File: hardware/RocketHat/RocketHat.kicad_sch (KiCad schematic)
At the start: 29 parts, among them J1 Conn_02x16_Top_Bottom, J2 Conn_02x16_Top_Bottom, Q2 MMBT2222A, U1 BMP390, U2 BMI088, U3 ADXL375BCCZ, U5 74HC688, U6 74HC245, U7 74HC245, U8 MAX-M10S

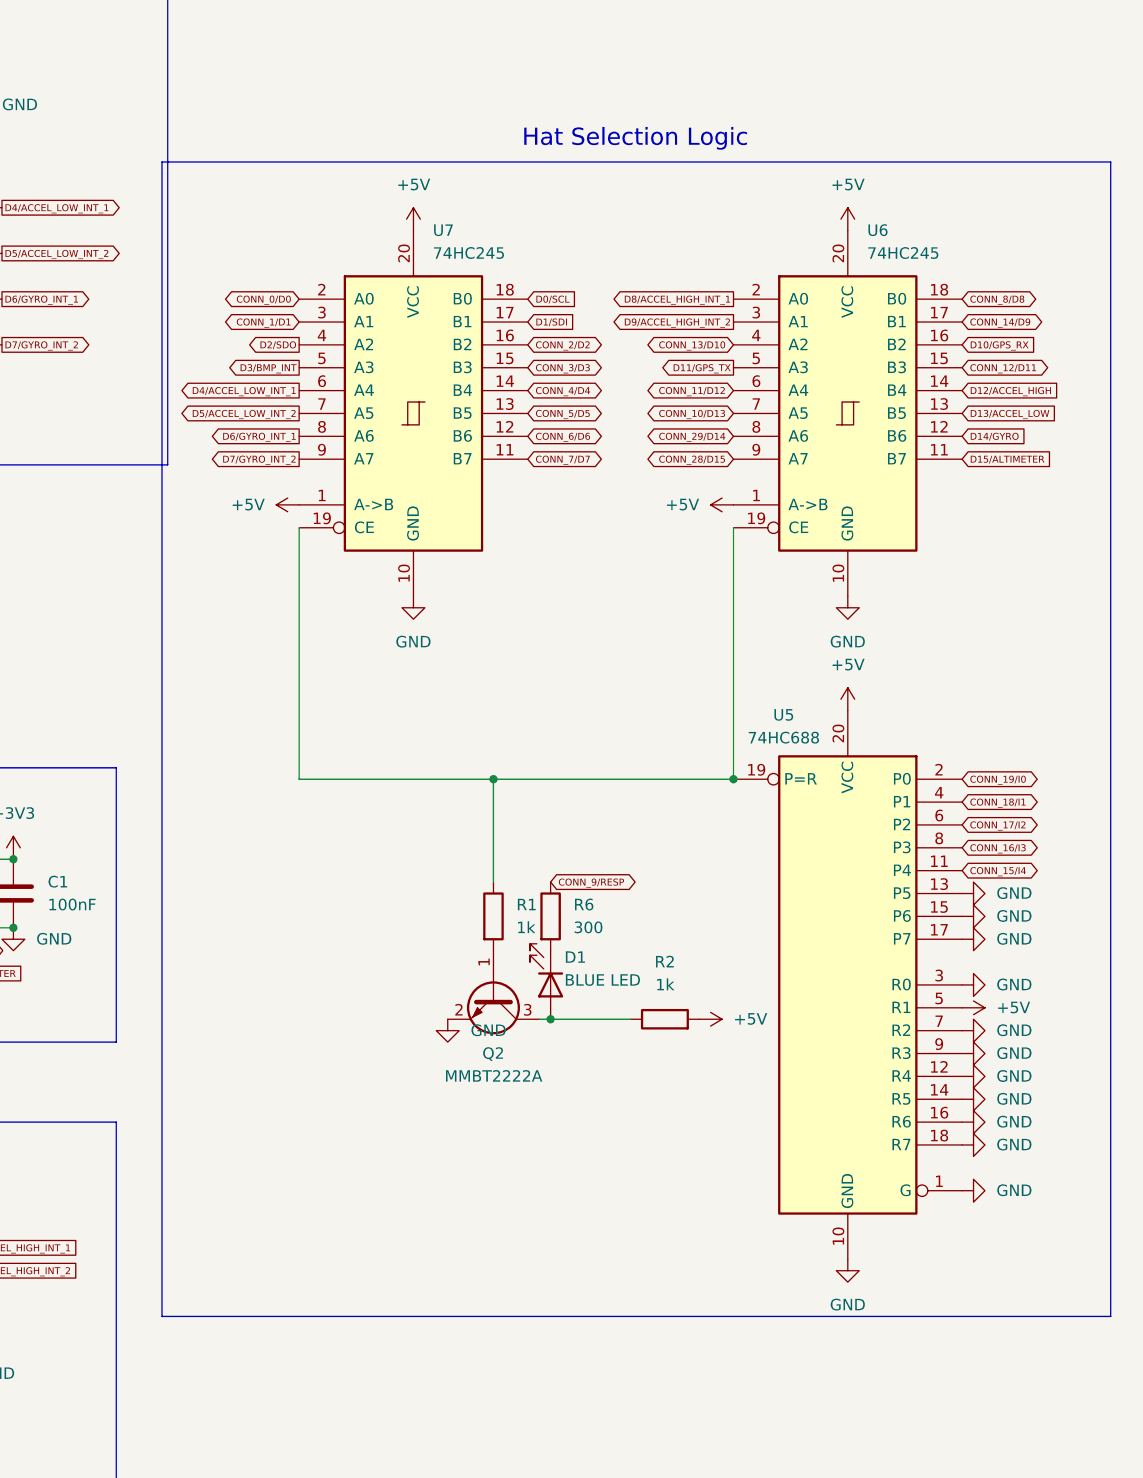
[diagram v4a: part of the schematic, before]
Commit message: Work more on traces for rocket hat and add dipswitch
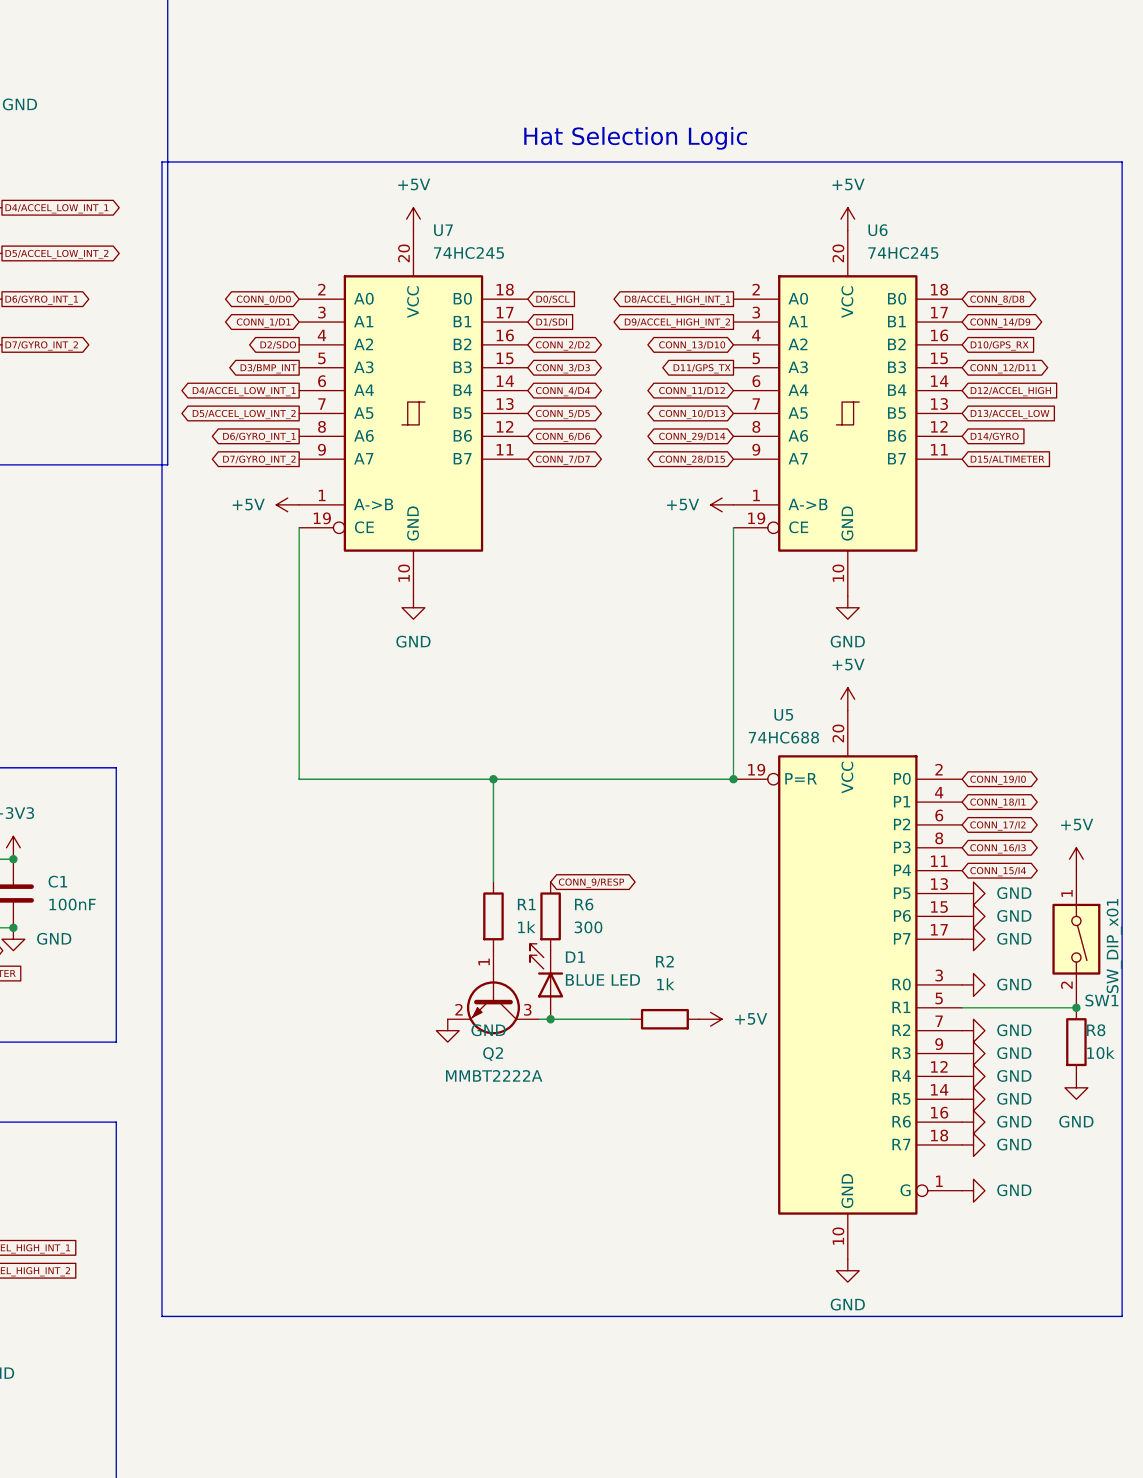
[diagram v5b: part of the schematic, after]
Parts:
- added R8: 10k, Resistor_SMD:R_0201_0603Metric, symbol Device:R
- added SW1: SW_DIP_x01, Button_Switch_SMD:SW_DIP_SPSTx01_Slide_Copal_CHS-01A_W5.08mm_P1.27mm_JPin, symbol Switch:SW_DIP_x01
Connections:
- net +5V: now also SW1.1; no longer U5.5 (R1)
- net GND: now also R8.2
- new net: R8.1, SW1.2, U5.5 (R1)
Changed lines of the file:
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@@
 	(rectangle
 		(start 176.53 38.1)
-		(end 281.94 166.37)
+		(end 283.21 166.37)
 		(stroke
 			(width 0)
@@
 	)
 	(junction
+		(at 278.13 132.08)
+		(diameter 0)
+		(color 0 0 0 0)
+	)
+	(junction
 		(at 76.2 46.99)
 		(diameter 0)
@@
 	(wire
 		(pts
+			(xy 265.43 132.08) (xy 278.13 132.08)
+		)
+		(stroke
+			(width 0)
+			(type default)
+		)
+	)
+	(wire
+		(pts
 			(xy 218.44 133.35) (xy 219.71 133.35)
 		)
@@
 	)
 	(symbol
-		(lib_id "power:+5V")
-		(at 265.43 132.08 270)
-		(unit 1)
-		(exclude_from_sim no)
-		(in_bom yes)
-		(on_board yes)
-		(dnp no)
-		(fields_autoplaced yes)
-		(property "Reference" "#PWR012"
-			(at 261.62 132.08 0)
-			(effects
-				(font
-					(size 1.27 1.27)
-				)
-				(hide yes)
-			)
-		)
-		(property "Value" "+5V"
-			(at 269.24 132.0799 90)
-			(effects
-				(font
-					(size 1.27 1.27)
-				)
-				(justify left)
-			)
-		)
-		(property "Footprint" ""
-			(at 265.43 132.08 0)
-			(effects
-				(font
-					(size 1.27 1.27)
-				)
-				(hide yes)
-			)
-		)
-		(property "Datasheet" ""
-			(at 265.43 132.08 0)
-			(effects
-				(font
-					(size 1.27 1.27)
-				)
-				(hide yes)
-			)
-		)
-		(property "Description" "Power symbol creates a global label with name \"+5V\""
-			(at 265.43 132.08 0)
-			(effects
-				(font
-					(size 1.27 1.27)
-				)
-				(hide yes)
-			)
-		)
-		(pin "1"
-		)
-		(instances
-			(project ""
-				(path "/988df97c-fca1-40e2-af98-331e3f3f354f"
-					(reference "#PWR012")
-					(unit 1)
-				)
-			)
-		)
-	)
-	(symbol
 		(lib_id "Device:R")
 		(at 76.2 43.18 0)
@@
 	)
 	(symbol
+		(lib_id "Device:R")
+		(at 278.13 135.89 0)
+		(unit 1)
+		(exclude_from_sim no)
+		(in_bom yes)
+		(on_board yes)
+		(dnp no)
+		(property "Reference" "R8"
+			(at 279.146 134.62 0)
+			(effects
+				(font
+					(size 1.27 1.27)
+				)
+				(justify left)
+			)
+		)
+		(property "Value" "10k"
+			(at 279.146 137.16 0)
+			(effects
+				(font
+					(size 1.27 1.27)
+				)
+				(justify left)
+			)
+		)
+		(property "Footprint" "Resistor_SMD:R_0201_0603Metric"
+			(at 276.352 135.89 90)
+			(effects
+				(font
+					(size 1.27 1.27)
+				)
+				(hide yes)
+			)
+		)
+		(property "Datasheet" "~"
+			(at 278.13 135.89 0)
+			(effects
+				(font
+					(size 1.27 1.27)
+				)
+				(hide yes)
+			)
+		)
+		(property "Description" "Resistor"
+			(at 278.13 135.89 0)
+			(effects
+				(font
+					(size 1.27 1.27)
+				)
+				(hide yes)
+			)
+		)
+		(pin "2"
+		)
+		(pin "1"
+		)
+		(instances
+			(project ""
+				(path "/988df97c-fca1-40e2-af98-331e3f3f354f"
+					(reference "R8")
+					(unit 1)
+				)
+			)
+		)
+	)
+	(symbol
 		(lib_id "Device:C")
 		(at 49.53 29.21 0)
@@
 	)
 	(symbol
+		(lib_id "power:+5V")
+		(at 278.13 116.84 0)
+		(unit 1)
+		(exclude_from_sim no)
+		(in_bom yes)
+		(on_board yes)
+		(dnp no)
+		(fields_autoplaced yes)
+		(property "Reference" "#PWR051"
+			(at 278.13 120.65 0)
+			(effects
+				(font
+					(size 1.27 1.27)
+				)
+				(hide yes)
+			)
+		)
+		(property "Value" "+5V"
+			(at 278.13 111.76 0)
+			(effects
+				(font
+					(size 1.27 1.27)
+				)
+			)
+		)
+		(property "Footprint" ""
+			(at 278.13 116.84 0)
+			(effects
+				(font
+					(size 1.27 1.27)
+				)
+				(hide yes)
+			)
+		)
+		(property "Datasheet" ""
+			(at 278.13 116.84 0)
+			(effects
+				(font
+					(size 1.27 1.27)
+				)
+				(hide yes)
+			)
+		)
+		(property "Description" "Power symbol creates a global label with name \"+5V\""
+			(at 278.13 116.84 0)
+			(effects
+				(font
+					(size 1.27 1.27)
+				)
+				(hide yes)
+			)
+		)
+		(pin "1"
+		)
+		(instances
+			(project "RocketHat"
+				(path "/988df97c-fca1-40e2-af98-331e3f3f354f"
+					(reference "#PWR051")
+					(unit 1)
+				)
+			)
+		)
+	)
+	(symbol
 		(lib_id "Device:C")
 		(at 76.2 50.8 0)
@@
 	)
 	(symbol
+		(lib_id "power:GND")
+		(at 278.13 139.7 0)
+		(unit 1)
+		(exclude_from_sim no)
+		(in_bom yes)
+		(on_board yes)
+		(dnp no)
+		(fields_autoplaced yes)
+		(property "Reference" "#PWR012"
+			(at 278.13 146.05 0)
+			(effects
+				(font
+					(size 1.27 1.27)
+				)
+				(hide yes)
+			)
+		)
+		(property "Value" "GND"
+			(at 278.13 144.78 0)
+			(effects
+				(font
+					(size 1.27 1.27)
+				)
+			)
+		)
+		(property "Footprint" ""
+			(at 278.13 139.7 0)
+			(effects
+				(font
+					(size 1.27 1.27)
+				)
+				(hide yes)
+			)
+		)
+		(property "Datasheet" ""
+			(at 278.13 139.7 0)
+			(effects
+				(font
+					(size 1.27 1.27)
+				)
+				(hide yes)
+			)
+		)
+		(property "Description" "Power symbol creates a global label with name \"GND\" , ground"
+			(at 278.13 139.7 0)
+			(effects
+				(font
+					(size 1.27 1.27)
+				)
+				(hide yes)
+			)
+		)
+		(pin "1"
+		)
+		(instances
+			(project "RocketHat"
+				(path "/988df97c-fca1-40e2-af98-331e3f3f354f"
+					(reference "#PWR012")
+					(unit 1)
+				)
+			)
+		)
+	)
+	(symbol
 		(lib_id "Device:R")
 		(at 219.71 121.92 0)
@@
 					(unit 1)
 				)
+			)
+		)
+	)
+	(symbol
+		(lib_id "Switch:SW_DIP_x01")
+		(at 278.13 124.46 270)
+		(unit 1)
+		(exclude_from_sim no)
+		(in_bom yes)
+		(on_board yes)
+		(dnp no)
+		(property "Reference" "SW1"
+			(at 282.956 131.318 90)
+			(effects
+				(font
+					(size 1.27 1.27)
+				)
+				(justify right)
+			)
+		)
+		(property "Value" "SW_DIP_x01"
+			(at 282.194 130.556 0)
+			(effects
+				(font
+					(size 1.27 1.27)
+				)
+				(justify right)
+			)
+		)
+		(property "Footprint" "Button_Switch_SMD:SW_DIP_SPSTx01_Slide_Copal_CHS-01A_W5.08mm_P1.27mm_JPin"
+			(at 278.13 124.46 0)
+			(effects
+				(font
+					(size 1.27 1.27)
+				)
+				(hide yes)
+			)
+		)
+		(property "Datasheet" "~"
+			(at 278.13 124.46 0)
+			(effects
+				(font
+					(size 1.27 1.27)
+				)
+				(hide yes)
+			)
+		)
+		(property "Description" "1x DIP Switch, Single Pole Single Throw (SPST) switch, small symbol"
+			(at 278.13 124.46 0)
+			(effects
+				(font
+					(size 1.27 1.27)
+				)
+				(hide yes)
+			)
+		)
+		(pin "2"
+		)
+		(pin "1"
+		)
+		(instances
+			(project ""
+				(path "/988df97c-fca1-40e2-af98-331e3f3f354f"
+					(reference "SW1")
+					(unit 1)
+				)

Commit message: rocket hat done
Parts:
- removed SW1: SW_DIP_x01, Button_Switch_SMD:SW_DIP_SPSTx01_Slide_Copal_CHS-01A_W5.08mm_P1.27mm_JPin, symbol Switch:SW_DIP_x01
- added TP1, TP2: TestPoint, TestPoint:TestPoint_Pad_1.5x1.5mm, symbol Connector:TestPoint
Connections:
- net +5V: now also TP2.1
- net at R8.1, U5.5 (R1): now also TP1.1
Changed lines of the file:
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@@
 	)
 	(junction
+		(at 278.13 132.08)
+		(diameter 0)
+		(color 0 0 0 0)
+	)
+	(junction
 		(at 82.55 163.83)
 		(diameter 0)
@@
 	)
 	(junction
-		(at 278.13 132.08)
-		(diameter 0)
-		(color 0 0 0 0)
-	)
-	(junction
 		(at 76.2 46.99)
 		(diameter 0)
@@
 	)
 	(symbol
+		(lib_id "Connector:TestPoint")
+		(at 278.13 132.08 0)
+		(unit 1)
+		(exclude_from_sim no)
+		(in_bom yes)
+		(on_board yes)
+		(dnp no)
+		(fields_autoplaced yes)
+		(property "Reference" "TP1"
+			(at 280.67 127.5079 0)
+			(effects
+				(font
+					(size 1.27 1.27)
+				)
+				(justify left)
+			)
+		)
+		(property "Value" "TestPoint"
+			(at 280.67 130.0479 0)
+			(effects
+				(font
+					(size 1.27 1.27)
+				)
+				(justify left)
+			)
+		)
+		(property "Footprint" "TestPoint:TestPoint_Pad_1.5x1.5mm"
+			(at 283.21 132.08 0)
+			(effects
+				(font
+					(size 1.27 1.27)
+				)
+				(hide yes)
+			)
+		)
+		(property "Datasheet" "~"
+			(at 283.21 132.08 0)
+			(effects
+				(font
+					(size 1.27 1.27)
+				)
+				(hide yes)
+			)
+		)
+		(property "Description" "test point"
+			(at 278.13 132.08 0)
+			(effects
+				(font
+					(size 1.27 1.27)
+				)
+				(hide yes)
+			)
+		)
+		(pin "1"
+		)
+		(instances
+			(project ""
+				(path "/988df97c-fca1-40e2-af98-331e3f3f354f"
+					(reference "TP1")
+					(unit 1)
+				)
+			)
+		)
+	)
+	(symbol
 		(lib_id "power:GND")
 		(at 153.67 171.45 0)
@@
 		(on_board yes)
 		(dnp no)
-		(fields_autoplaced yes)
 		(property "Reference" "#PWR037"
 			(at 133.35 67.31 0)
@@
 		)
 		(property "Value" "GND"
-			(at 135.89 62.2299 0)
+			(at 131.826 64.77 0)
 			(effects
 				(font
@@
 	)
 	(symbol
-		(lib_id "power:GND")
-		(at 265.43 121.92 90)
+		(lib_id "Connector:TestPoint")
+		(at 278.13 116.84 180)
 		(unit 1)
 		(exclude_from_sim no)
@@
 		(dnp no)
 		(fields_autoplaced yes)
-		(property "Reference" "#PWR02"
-			(at 271.78 121.92 0)
+		(property "Reference" "TP2"
+			(at 280.67 118.8719 0)
 			(effects
 				(font
 					(size 1.27 1.27)
 				)
-				(hide yes)
+				(justify right)
 			)
 		)
-		(property "Value" "GND"
-			(at 269.24 121.9199 90)
+		(property "Value" "TestPoint"
+			(at 280.67 121.4119 0)
 			(effects
 				(font
@@
 			)
 		)
-		(property "Footprint" ""
-			(at 265.43 121.92 0)
+		(property "Footprint" "TestPoint:TestPoint_Pad_1.5x1.5mm"
+			(at 273.05 116.84 0)
 			(effects
 				(font
@@
 			)
 		)
-		(property "Datasheet" ""
-			(at 265.43 121.92 0)
+		(property "Datasheet" "~"
+			(at 273.05 116.84 0)
 			(effects
 				(font
@@
 			)
 		)
-		(property "Description" "Power symbol creates a global label with name \"GND\" , ground"
-			(at 265.43 121.92 0)
+		(property "Description" "test point"
+			(at 278.13 116.84 0)
 			(effects
 				(font
@@
 			(project "RocketHat"
 				(path "/988df97c-fca1-40e2-af98-331e3f3f354f"
-					(reference "#PWR02")
+					(reference "TP2")
 					(unit 1)
 				)
@@
 	)
 	(symbol
-		(lib_id "power:+5V")
-		(at 240.03 76.2 90)
+		(lib_id "power:GND")
+		(at 265.43 121.92 90)
 		(unit 1)
 		(exclude_from_sim no)
@@
 		(dnp no)
 		(fields_autoplaced yes)
-		(property "Reference" "#PWR018"
-			(at 243.84 76.2 0)
+		(property "Reference" "#PWR02"
+			(at 271.78 121.92 0)
 			(effects
 				(font
@@
 			)
 		)
-		(property "Value" "+5V"
-			(at 236.22 76.1999 90)
+		(property "Value" "GND"
+			(at 269.24 121.9199 90)
 			(effects
 				(font
 					(size 1.27 1.27)
 				)
-				(justify left)
+				(justify right)
 			)
 		)
 		(property "Footprint" ""
-			(at 240.03 76.2 0)
+			(at 265.43 121.92 0)
 			(effects
 				(font
@@
 		)
 		(property "Datasheet" ""
-			(at 240.03 76.2 0)
+			(at 265.43 121.92 0)
 			(effects
 				(font
@@
 			)
 		)
-		(property "Description" "Power symbol creates a global label with name \"+5V\""
-			(at 240.03 76.2 0)
+		(property "Description" "Power symbol creates a global label with name \"GND\" , ground"
+			(at 265.43 121.92 0)
 			(effects
 				(font
@@
 			(project "RocketHat"
 				(path "/988df97c-fca1-40e2-af98-331e3f3f354f"
-					(reference "#PWR018")
+					(reference "#PWR02")
 					(unit 1)
 				)
@@
 	)
 	(symbol
-		(lib_id "Switch:SW_DIP_x01")
-		(at 278.13 124.46 270)
+		(lib_id "power:+5V")
+		(at 240.03 76.2 90)
 		(unit 1)
 		(exclude_from_sim no)
@@
 		(on_board yes)
 		(dnp no)
-		(property "Reference" "SW1"
-			(at 282.956 131.318 90)
+		(fields_autoplaced yes)
+		(property "Reference" "#PWR018"
+			(at 243.84 76.2 0)
 			(effects
 				(font
 					(size 1.27 1.27)
 				)
-				(justify right)
+				(hide yes)
 			)
 		)
-		(property "Value" "SW_DIP_x01"
-			(at 282.194 130.556 0)
+		(property "Value" "+5V"
+			(at 236.22 76.1999 90)
 			(effects
 				(font
 					(size 1.27 1.27)
 				)
-				(justify right)
+				(justify left)
 			)
 		)
-		(property "Footprint" "Button_Switch_SMD:SW_DIP_SPSTx01_Slide_Copal_CHS-01A_W5.08mm_P1.27mm_JPin"
-			(at 278.13 124.46 0)
+		(property "Footprint" ""
+			(at 240.03 76.2 0)
 			(effects
 				(font
@@
 			)
 		)
-		(property "Datasheet" "~"
-			(at 278.13 124.46 0)
+		(property "Datasheet" ""
+			(at 240.03 76.2 0)
 			(effects
 				(font
@@
 			)
 		)
-		(property "Description" "1x DIP Switch, Single Pole Single Throw (SPST) switch, small symbol"
-			(at 278.13 124.46 0)
+		(property "Description" "Power symbol creates a global label with name \"+5V\""
+			(at 240.03 76.2 0)
 			(effects
 				(font
@@
 			)
 		)
-		(pin "2"
-		)
 		(pin "1"
 		)
 		(instances
-			(project ""
+			(project "RocketHat"
 				(path "/988df97c-fca1-40e2-af98-331e3f3f354f"
-					(reference "SW1")
+					(reference "#PWR018")
 					(unit 1)
 				)

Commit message: sanity checked, ready for production
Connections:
- net +5V: now also U5.5 (R1)
- net GND: no longer U5.3 (R0)
- net at R8.1, TP1.1: now also U5.3 (R0); no longer U5.5 (R1)
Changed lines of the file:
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@@
 	)
 	(junction
-		(at 278.13 132.08)
-		(diameter 0)
-		(color 0 0 0 0)
-	)
-	(junction
 		(at 82.55 163.83)
 		(diameter 0)
@@
 	)
 	(junction
+		(at 278.13 132.08)
+		(diameter 0)
+		(color 0 0 0 0)
+	)
+	(junction
 		(at 156.21 30.48)
 		(diameter 0)
@@
 	(wire
 		(pts
+			(xy 275.59 129.54) (xy 265.43 129.54)
+		)
+		(stroke
+			(width 0)
+			(type default)
+		)
+	)
+	(wire
+		(pts
 			(xy 69.85 163.83) (xy 69.85 158.75)
 		)
@@
 	(wire
 		(pts
+			(xy 278.13 132.08) (xy 275.59 132.08)
+		)
+		(stroke
+			(width 0)
+			(type default)
+		)
+	)
+	(wire
+		(pts
 			(xy 213.36 118.11) (xy 213.36 106.68)
 		)
@@
 	(wire
 		(pts
+			(xy 275.59 132.08) (xy 275.59 129.54)
+		)
+		(stroke
+			(width 0)
+			(type default)
+		)
+	)
+	(wire
+		(pts
 			(xy 240.03 78.74) (xy 240.03 106.68)
 		)
@@
 	(wire
 		(pts
-			(xy 265.43 132.08) (xy 278.13 132.08)
-		)
-		(stroke
-			(width 0)
-			(type default)
-		)
-	)
-	(wire
-		(pts
 			(xy 218.44 133.35) (xy 219.71 133.35)
 		)
@@
 	)
 	(symbol
-		(lib_id "power:GND")
-		(at 265.43 129.54 90)
-		(unit 1)
-		(exclude_from_sim no)
-		(in_bom yes)
-		(on_board yes)
-		(dnp no)
-		(fields_autoplaced yes)
-		(property "Reference" "#PWR04"
-			(at 271.78 129.54 0)
-			(effects
-				(font
-					(size 1.27 1.27)
-				)
-				(hide yes)
-			)
-		)
-		(property "Value" "GND"
-			(at 269.24 129.5399 90)
-			(effects
-				(font
-					(size 1.27 1.27)
-				)
-				(justify right)
-			)
-		)
-		(property "Footprint" ""
-			(at 265.43 129.54 0)
-			(effects
-				(font
-					(size 1.27 1.27)
-				)
-				(hide yes)
-			)
-		)
-		(property "Datasheet" ""
-			(at 265.43 129.54 0)
-			(effects
-				(font
-					(size 1.27 1.27)
-				)
-				(hide yes)
-			)
-		)
-		(property "Description" "Power symbol creates a global label with name \"GND\" , ground"
-			(at 265.43 129.54 0)
-			(effects
-				(font
-					(size 1.27 1.27)
-				)
-				(hide yes)
-			)
-		)
-		(pin "1"
-		)
-		(instances
-			(project "RocketHat"
-				(path "/988df97c-fca1-40e2-af98-331e3f3f354f"
-					(reference "#PWR04")
-					(unit 1)
-				)
-			)
-		)
-	)
-	(symbol
 		(lib_id "Device:R")
 		(at 213.36 121.92 0)
@@
 					(unit 1)
 				)
+			)
+		)
+	)
+	(symbol
+		(lib_id "power:+5V")
+		(at 265.43 132.08 270)
+		(unit 1)
+		(exclude_from_sim no)
+		(in_bom yes)
+		(on_board yes)
+		(dnp no)
+		(fields_autoplaced yes)
+		(property "Reference" "#PWR04"
+			(at 261.62 132.08 0)
+			(effects
+				(font
+					(size 1.27 1.27)
+				)
+				(hide yes)
+			)
+		)
+		(property "Value" "+5V"
+			(at 269.24 132.0799 90)
+			(effects
+				(font
+					(size 1.27 1.27)
+				)
+				(justify left)
+			)
+		)
+		(property "Footprint" ""
+			(at 265.43 132.08 0)
+			(effects
+				(font
+					(size 1.27 1.27)
+				)
+				(hide yes)
+			)
+		)
+		(property "Datasheet" ""
+			(at 265.43 132.08 0)
+			(effects
+				(font
+					(size 1.27 1.27)
+				)
+				(hide yes)
+			)
+		)
+		(property "Description" "Power symbol creates a global label with name \"+5V\""
+			(at 265.43 132.08 0)
+			(effects
+				(font
+					(size 1.27 1.27)
+				)
+				(hide yes)
+			)
+		)
+		(pin "1"
+		)
+		(instances
+			(project "RocketHat"
+				(path "/988df97c-fca1-40e2-af98-331e3f3f354f"
+					(reference "#PWR04")
+					(unit 1)
+				)
